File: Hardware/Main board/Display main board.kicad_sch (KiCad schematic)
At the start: 8 parts, among them J1 Board to Board

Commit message: Update GND symbols
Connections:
- net GND renamed PGND
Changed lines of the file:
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@@
+	(wire
+		(pts
+			(xy 340.36 82.55) (xy 339.09 82.55)
+		)
+		(stroke
+			(width 0)
+			(type default)
+		)
+	)
 	(wire
 		(pts
@@
 	(global_label "MB_CLK_LOW"
 		(shape input)
-		(at 339.09 82.55 0)
+		(at 340.36 82.55 0)
 		(fields_autoplaced yes)
 		(effects
@@
 		)
 		(property "Intersheetrefs" "${INTERSHEET_REFS}"
-			(at 354.1099 82.55 0)
+			(at 355.3799 82.55 0)
 			(effects
 				(font
@@
 	)
 	(symbol
+		(lib_id "BQ25895-accurate:PGND")
+		(at 193.04 147.32 0)
+		(unit 1)
+		(exclude_from_sim no)
+		(in_bom no)
+		(on_board no)
+		(dnp no)
+		(fields_autoplaced yes)
+		(property "Reference" "#PWR035"
+			(at 192.786 147.574 0)
+			(effects
+				(font
+					(size 1.27 1.27)
+				)
+				(hide yes)
+			)
+		)
+		(property "Value" "PGND"
+			(at 193.04 152.4 0)
+			(effects
+				(font
+					(size 1.27 1.27)
+				)
+			)
+		)
+		(property "Footprint" ""
+			(at 193.04 147.32 0)
+			(effects
+				(font
+					(size 1.27 1.27)
+				)
+				(hide yes)
+			)
+		)
+		(property "Datasheet" ""
+			(at 193.04 147.32 0)
+			(effects
+				(font
+					(size 1.27 1.27)
+				)
+				(hide yes)
+			)
+		)
+		(property "Description" ""
+			(at 193.04 147.32 0)
+			(effects
+				(font
+					(size 1.27 1.27)
+				)
+				(hide yes)
+			)
+		)
+		(pin ""
+		)
+		(instances
+			(project ""
+				(path "/e5119d15-74fb-4259-abbc-5cab1f368532"
+					(reference "#PWR035")
+					(unit 1)
+				)
+			)
+		)
+	)
+	(symbol
+		(lib_id "BQ25895-accurate:PGND")
+		(at 205.74 147.32 0)
+		(unit 1)
+		(exclude_from_sim no)
+		(in_bom no)
+		(on_board no)
+		(dnp no)
+		(fields_autoplaced yes)
+		(property "Reference" "#PWR037"
+			(at 205.486 147.574 0)
+			(effects
+				(font
+					(size 1.27 1.27)
+				)
+				(hide yes)
+			)
+		)
+		(property "Value" "PGND"
+			(at 205.74 152.4 0)
+			(effects
+				(font
+					(size 1.27 1.27)
+				)
+			)
+		)
+		(property "Footprint" ""
+			(at 205.74 147.32 0)
+			(effects
+				(font
+					(size 1.27 1.27)
+				)
+				(hide yes)
+			)
+		)
+		(property "Datasheet" ""
+			(at 205.74 147.32 0)
+			(effects
+				(font
+					(size 1.27 1.27)
+				)
+				(hide yes)
+			)
+		)
+		(property "Description" ""
+			(at 205.74 147.32 0)
+			(effects
+				(font
+					(size 1.27 1.27)
+				)
+				(hide yes)
+			)
+		)
+		(pin ""
+		)
+		(instances
+			(project ""
+				(path "/e5119d15-74fb-4259-abbc-5cab1f368532"
+					(reference "#PWR037")
+					(unit 1)
+				)
+			)
+		)
+	)
+	(symbol
 		(lib_id "Mechanical:MountingHole")
 		(at 201.93 101.6 0)
@@
 					(unit 1)
 				)
-			)
-		)
-	)
-	(symbol
-		(lib_id "power:GND")
-		(at 205.74 147.32 0)
-		(unit 1)
-		(exclude_from_sim no)
-		(in_bom yes)
-		(on_board yes)
-		(dnp no)
-		(fields_autoplaced yes)
-		(property "Reference" "#PWR03"
-			(at 205.74 153.67 0)
-			(effects
-				(font
-					(size 1.27 1.27)
-				)
-				(hide yes)
-			)
-		)
-		(property "Value" "GND"
-			(at 205.74 152.4 0)
-			(effects
-				(font
-					(size 1.27 1.27)
-				)
-			)
-		)
-		(property "Footprint" ""
-			(at 205.74 147.32 0)
-			(effects
-				(font
-					(size 1.27 1.27)
-				)
-				(hide yes)
-			)
-		)
-		(property "Datasheet" ""
-			(at 205.74 147.32 0)
-			(effects
-				(font
-					(size 1.27 1.27)
-				)
-				(hide yes)
-			)
-		)
-		(property "Description" "Power symbol creates a global label with name \"GND\" , ground"
-			(at 205.74 147.32 0)
-			(effects
-				(font
-					(size 1.27 1.27)
-				)
-				(hide yes)
-			)
-		)
-		(pin "1"
-		)
-		(instances
-			(project "Minibadge Display 5x3"
-				(path "/e5119d15-74fb-4259-abbc-5cab1f368532"
-					(reference "#PWR03")
-					(unit 1)
-				)
-			)
-		)
-	)
-	(symbol
-		(lib_id "power:GND")
-		(at 193.04 147.32 0)
-		(unit 1)
-		(exclude_from_sim no)
-		(in_bom yes)
-		(on_board yes)
-		(dnp no)
-		(fields_autoplaced yes)
-		(property "Reference" "#PWR02"
-			(at 193.04 153.67 0)
-			(effects
-				(font
-					(size 1.27 1.27)
-				)
-				(hide yes)
-			)
-		)
-		(property "Value" "GND"
-			(at 193.04 152.4 0)
-			(effects
-				(font
-					(size 1.27 1.27)
-				)
-			)
-		)
-		(property "Footprint" ""
-			(at 193.04 147.32 0)
-			(effects
-				(font
-					(size 1.27 1.27)
-				)
-				(hide yes)
-			)
-		)
-		(property "Datasheet" ""
-			(at 193.04 147.32 0)
-			(effects
-				(font
-					(size 1.27 1.27)
-				)
-				(hide yes)
-			)
-		)
-		(property "Description" "Power symbol creates a global label with name \"GND\" , ground"
-			(at 193.04 147.32 0)
-			(effects
-				(font
-					(size 1.27 1.27)
-				)
-				(hide yes)
-			)
-		)
-		(pin "1"
-		)
-		(instances
-			(project "Minibadge Display 5x3"
-				(path "/e5119d15-74fb-4259-abbc-5cab1f368532"
-					(reference "#PWR02")
-					(unit 1)
-				)

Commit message: refactor PCB for new BMS layout
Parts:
- H1: footprint (none) -> MountingHole:MountingHole_2.2mm_M2
- H2: renamed from H5; footprint (none) -> MountingHole:MountingHole_2.2mm_M2
- H3: renamed from H2; footprint (none) -> MountingHole:MountingHole_2.2mm_M2
- H4: renamed from H6; footprint (none) -> MountingHole:MountingHole_2.2mm_M2
- H5: renamed from H3; footprint (none) -> MountingHole:MountingHole_2.2mm_M2
- H6: renamed from H7; footprint (none) -> MountingHole:MountingHole_2.2mm_M2
- H7: renamed from H4; footprint (none) -> MountingHole:MountingHole_2.2mm_M2
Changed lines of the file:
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@@
 		(dnp no)
 		(fields_autoplaced yes)
-		(property "Reference" "H2"
+		(property "Reference" "H3"
 			(at 182.88 93.9799 0)
 			(effects
@@
 			)
 		)
-		(property "Footprint" ""
+		(property "Footprint" "MountingHole:MountingHole_2.2mm_M2"
 			(at 180.34 95.25 0)
 			(effects
@@
 			(project ""
 				(path "/e5119d15-74fb-4259-abbc-5cab1f368532"
-					(reference "H2")
+					(reference "H3")
 					(unit 1)
 				)
@@
 		(dnp no)
 		(fields_autoplaced yes)
-		(property "Reference" "H5"
+		(property "Reference" "H2"
 			(at 204.47 87.6299 0)
 			(effects
@@
 			)
 		)
-		(property "Footprint" ""
+		(property "Footprint" "MountingHole:MountingHole_2.2mm_M2"
 			(at 201.93 88.9 0)
 			(effects
@@
 			(project ""
 				(path "/e5119d15-74fb-4259-abbc-5cab1f368532"
-					(reference "H5")
+					(reference "H2")
 					(unit 1)
 				)
@@
 		(dnp no)
 		(fields_autoplaced yes)
-		(property "Reference" "H3"
+		(property "Reference" "H5"
 			(at 182.88 100.3299 0)
 			(effects
@@
 			)
 		)
-		(property "Footprint" ""
+		(property "Footprint" "MountingHole:MountingHole_2.2mm_M2"
 			(at 180.34 101.6 0)
 			(effects
@@
 			(project ""
 				(path "/e5119d15-74fb-4259-abbc-5cab1f368532"
-					(reference "H3")
+					(reference "H5")
 					(unit 1)
 				)
@@
 		(dnp no)
 		(fields_autoplaced yes)
-		(property "Reference" "#PWR035"
+		(property "Reference" "#PWR02"
 			(at 192.786 147.574 0)
 			(effects
@@
 			(project ""
 				(path "/e5119d15-74fb-4259-abbc-5cab1f368532"
-					(reference "#PWR035")
+					(reference "#PWR02")
 					(unit 1)
 				)
@@
 		(dnp no)
 		(fields_autoplaced yes)
-		(property "Reference" "#PWR037"
+		(property "Reference" "#PWR03"
 			(at 205.486 147.574 0)
 			(effects
@@
 			(project ""
 				(path "/e5119d15-74fb-4259-abbc-5cab1f368532"
-					(reference "#PWR037")
+					(reference "#PWR03")
 					(unit 1)
 				)
@@
 		(dnp no)
 		(fields_autoplaced yes)
-		(property "Reference" "H7"
+		(property "Reference" "H6"
 			(at 204.47 100.3299 0)
 			(effects
@@
 			)
 		)
-		(property "Footprint" ""
+		(property "Footprint" "MountingHole:MountingHole_2.2mm_M2"
 			(at 201.93 101.6 0)
 			(effects
@@
 			(project "Display main board"
 				(path "/e5119d15-74fb-4259-abbc-5cab1f368532"
-					(reference "H7")
+					(reference "H6")
 					(unit 1)
 				)
@@
 			)
 		)
-		(property "Footprint" ""
+		(property "Footprint" "MountingHole:MountingHole_2.2mm_M2"
 			(at 180.34 88.9 0)
 			(effects
@@
 		(dnp no)
 		(fields_autoplaced yes)
-		(property "Reference" "H6"
+		(property "Reference" "H4"
 			(at 204.47 93.9799 0)
 			(effects
@@
 			)
 		)
-		(property "Footprint" ""
+		(property "Footprint" "MountingHole:MountingHole_2.2mm_M2"
 			(at 201.93 95.25 0)
 			(effects
@@
 			(project "Display main board"
 				(path "/e5119d15-74fb-4259-abbc-5cab1f368532"
-					(reference "H6")
+					(reference "H4")
 					(unit 1)
 				)
@@
 		(dnp no)
 		(fields_autoplaced yes)
-		(property "Reference" "H4"
+		(property "Reference" "H7"
 			(at 182.88 106.6799 0)
 			(effects
@@
 			)
 		)
-		(property "Footprint" ""
+		(property "Footprint" "MountingHole:MountingHole_2.2mm_M2"
 			(at 180.34 107.95 0)
 			(effects
@@
 			(project ""
 				(path "/e5119d15-74fb-4259-abbc-5cab1f368532"
-					(reference "H4")
-					(unit 1)
-				)
+					(reference "H7")
+					(unit 1)
+				)

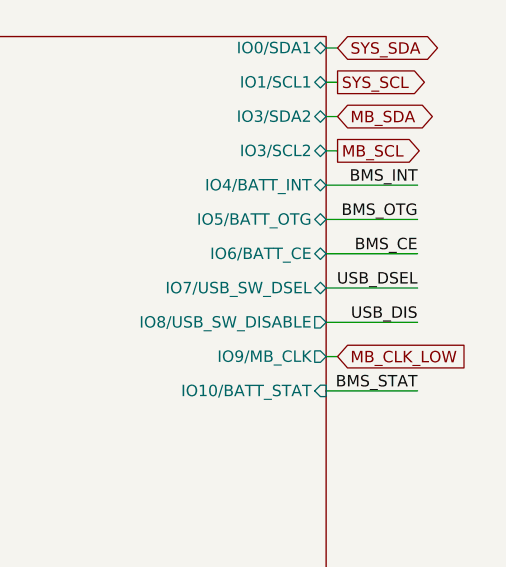
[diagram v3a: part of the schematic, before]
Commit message: All components routed
- broke out resistor network into individual resistors
- AGND tied to PGND by BMS
- repositioned GPIO positions
- length-matched USB to within 0.1mm
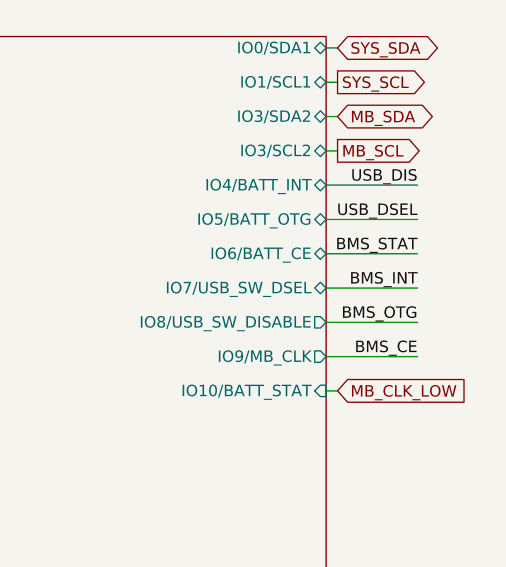
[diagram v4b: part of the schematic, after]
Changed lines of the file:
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@@
+	(wire
+		(pts
+			(xy 340.36 86.36) (xy 339.09 86.36)
+		)
+		(stroke
+			(width 0)
+			(type default)
+		)
+	)
 	(wire
 		(pts
@@
 	(wire
 		(pts
-			(xy 339.09 86.36) (xy 349.25 86.36)
-		)
-		(stroke
-			(width 0)
-			(type default)
-		)
-	)
-	(wire
-		(pts
 			(xy 270.51 77.47) (xy 285.75 77.47)
 		)
@@
 	(wire
 		(pts
-			(xy 340.36 82.55) (xy 339.09 82.55)
+			(xy 349.25 82.55) (xy 339.09 82.55)
 		)
 		(stroke
@@
 	)
 	(label "BMS_INT"
-		(at 349.25 63.5 180)
+		(at 349.25 74.93 180)
 		(effects
 			(font
@@
 	)
 	(label "BMS_OTG"
-		(at 349.25 67.31 180)
+		(at 349.25 78.74 180)
 		(effects
 			(font
@@
 	)
 	(label "BMS_STAT"
-		(at 349.25 86.36 180)
+		(at 349.25 71.12 180)
 		(effects
 			(font
@@
 	)
 	(label "USB_DSEL"
-		(at 349.25 74.93 180)
+		(at 349.25 67.31 180)
 		(effects
 			(font
@@
 	)
 	(label "USB_DIS"
-		(at 349.25 78.74 180)
+		(at 349.25 63.5 180)
 		(effects
 			(font
@@
 	)
 	(label "BMS_CE"
-		(at 349.25 71.12 180)
+		(at 349.25 82.55 180)
 		(effects
 			(font
@@
 	(global_label "MB_CLK_LOW"
 		(shape input)
-		(at 340.36 82.55 0)
+		(at 340.36 86.36 0)
 		(fields_autoplaced yes)
 		(effects
@@
 		)
 		(property "Intersheetrefs" "${INTERSHEET_REFS}"
-			(at 355.3799 82.55 0)
+			(at 355.3799 86.36 0)
 			(effects
 				(font
